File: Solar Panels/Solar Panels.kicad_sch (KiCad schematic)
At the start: 66 parts, among them J2 5040500891

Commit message: Modifications For 2U Panels
Made structural modifications to suit Brett's structure and tried to improve the PCB board based on Parker's suggestions. Schematic is extremely wonky right now but will try to fix it ASAP.
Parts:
- removed CR1, CR10, CR11, CR12, CR13, CR14, CR15, CR16, CR17, CR18, CR19, CR2, CR20, CR21, CR22, CR23, CR24, CR25, CR26, CR27, CR28, CR29, CR3, CR30, CR31, CR32, CR33, CR34, CR35, CR36, CR37, CR38, CR39, CR4, CR40, CR41, CR5, CR6, CR7, CR8, CR9: S3BB, SMB_DIO, symbol Calgary2Space:S3BB-13-F
- removed U1, U10, U11, U12, U13, U14, U15, U16, U17, U18, U19, U2, U20, U21, U22, U23, U24, U3, U4, U5, U6, U7, U8, U9: ~, Calgary2Space:TrisolX Solar Wings, symbol Calgary2Space:Solar_Panels
- added CR1, CR10, CR11, CR12, CR13, CR14, CR15, CR16, CR17, CR18, CR19, CR2, CR20, CR21, CR22, CR23, CR24, CR25, CR26, CR27, CR28, CR29, CR3, CR30, CR31, CR32, CR33, CR34, CR35, CR36, CR37, CR38, CR39, CR4, CR40, CR41, CR42, CR43, CR44, CR45, CR46, CR47, CR48, CR49, CR5, CR50, CR51, CR6, CR7, CR8, CR9: S3B_R1_00001, Solar Panel Library:SMC&slash_DO-214AB_PNJ, symbol Lib:S3B_R1_00001
- added H1, H2, H3, H4, H5, H6, H7, H8: MountingHole_Pad, MountingHole:MountingHole_3.2mm_M3_DIN965_Pad, symbol Mechanical:MountingHole_Pad
- added JP1, JP2, JP3, JP4, JP5, JP6, JP7, JP8: Jumper_2_Open, Jumper:SolderJumper-2_P1.3mm_Open_Pad1.0x1.5mm, symbol Jumper:Jumper_2_Open
- added SC1, SC10, SC11, SC12, SC13, SC14, SC15, SC16, SC17, SC18, SC19, SC2, SC20, SC21, SC22, SC23, SC24, SC25, SC26, SC27, SC28, SC29, SC3, SC30, SC4, SC5, SC6, SC7, SC8, SC9: Solar_Cell, Solar Panel Library:TrisolX Solar Wings, symbol Device:Solar_Cell
- J2: footprint CON_5040500891 -> Solar Panel Library:5040500891
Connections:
- net +VDC: now also CR1.1
- net GND: now also CR11.2, CR12.2, CR20.2, CR26.2, CR31.2, CR36.2, CR41.2, CR46.2, CR51.2, CR6.2, JP1.2 (B), JP2.2 (B), JP3.2 (B), JP4.2 (B), JP5.2 (B), JP6.2 (B), JP7.2 (B), JP8.2 (B), SC12.2 (-), SC15.2 (-), SC18.2 (-), SC21.2 (-), SC24.2 (-), SC27.2 (-), SC3.2 (-), SC30.2 (-), SC6.2 (-), SC9.2 (-)
- new net: CR1.2, CR16.1, CR2.1, CR21.1, CR22.1, CR27.1, CR32.1, CR37.1, CR44.1, CR49.1, CR8.1, SC1.1 (+), SC10.1 (+), SC13.1 (+), SC16.1 (+), SC19.1 (+), SC22.1 (+), SC25.1 (+), SC28.1 (+), SC4.1 (+), SC7.1 (+)
- new net: CR32.2, CR33.1, SC19.2 (-)
- new net: CR13.1, CR14.2, SC8.2 (-)
- new net: CR12.1, CR13.2, SC9.1 (+)
- new net: CR48.1, CR50.2, SC29.2 (-)
- new net: CR48.2, CR51.1, SC30.1 (+)
- new net: CR7.1, CR8.2, SC4.2 (-)
- new net: H4.1, JP4.1 (A)
- new net: CR7.2, CR9.1, SC5.1 (+)
- new net: CR10.1, CR9.2, SC5.2 (-)
- new net: CR37.2, CR38.1, SC22.2 (-)
- new net: H5.1, JP5.1 (A)
- new net: H6.1, JP6.1 (A)
- new net: CR47.2, CR50.1, SC29.1 (+)
- new net: H2.1, JP2.1 (A)
- new net: CR38.2, CR39.1, SC23.1 (+)
- new net: H8.1, JP8.1 (A)
- new net: H1.1, JP1.1 (A)
- new net: CR42.1, CR44.2, SC25.2 (-)
- new net: CR42.2, CR45.1, SC26.1 (+)
- new net: CR5.2, CR6.1, SC3.1 (+)
- new net: CR22.2, CR23.1, SC13.2 (-)
- new net: CR33.2, CR34.1, SC20.1 (+)
- new net: CR34.2, CR35.1, SC20.2 (-)
- new net: CR23.2, CR24.1, SC14.1 (+)
- new net: CR24.2, CR25.1, SC14.2 (-)
- new net: CR17.2, CR18.1, SC11.1 (+)
- new net: CR18.2, CR19.1, SC11.2 (-)
- new net: CR17.1, CR21.2, SC10.2 (-)
- new net: CR28.2, CR29.1, SC17.1 (+)
- new net: CR29.2, CR30.1, SC17.2 (-)
- new net: CR4.2, CR5.1, SC2.2 (-)
- new net: CR25.2, CR26.1, SC15.1 (+)
- new net: CR19.2, CR20.1, SC12.1 (+)
- new net: CR14.1, CR15.2, SC8.1 (+)
- new net: H7.1, JP7.1 (A)
- new net: CR40.2, CR41.1, SC24.1 (+)
- new net: CR43.1, CR45.2, SC26.2 (-)
- new net: CR43.2, CR46.1, SC27.1 (+)
- new net: CR27.2, CR28.1, SC16.2 (-)
- new net: CR30.2, CR31.1, SC18.1 (+)
- new net: CR47.1, CR49.2, SC28.2 (-)
- new net: H3.1, JP3.1 (A)
- new net: CR2.2, CR3.1, SC1.2 (-)
- new net: CR35.2, CR36.1, SC21.1 (+)
- new net: CR39.2, CR40.1, SC23.2 (-)
- new net: CR3.2, CR4.1, SC2.1 (+)
- new net: CR15.1, CR16.2, SC7.2 (-)
- new net: CR10.2, CR11.1, SC6.1 (+)
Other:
- note added: "Mounting Holes"
- moved on the sheet: J2

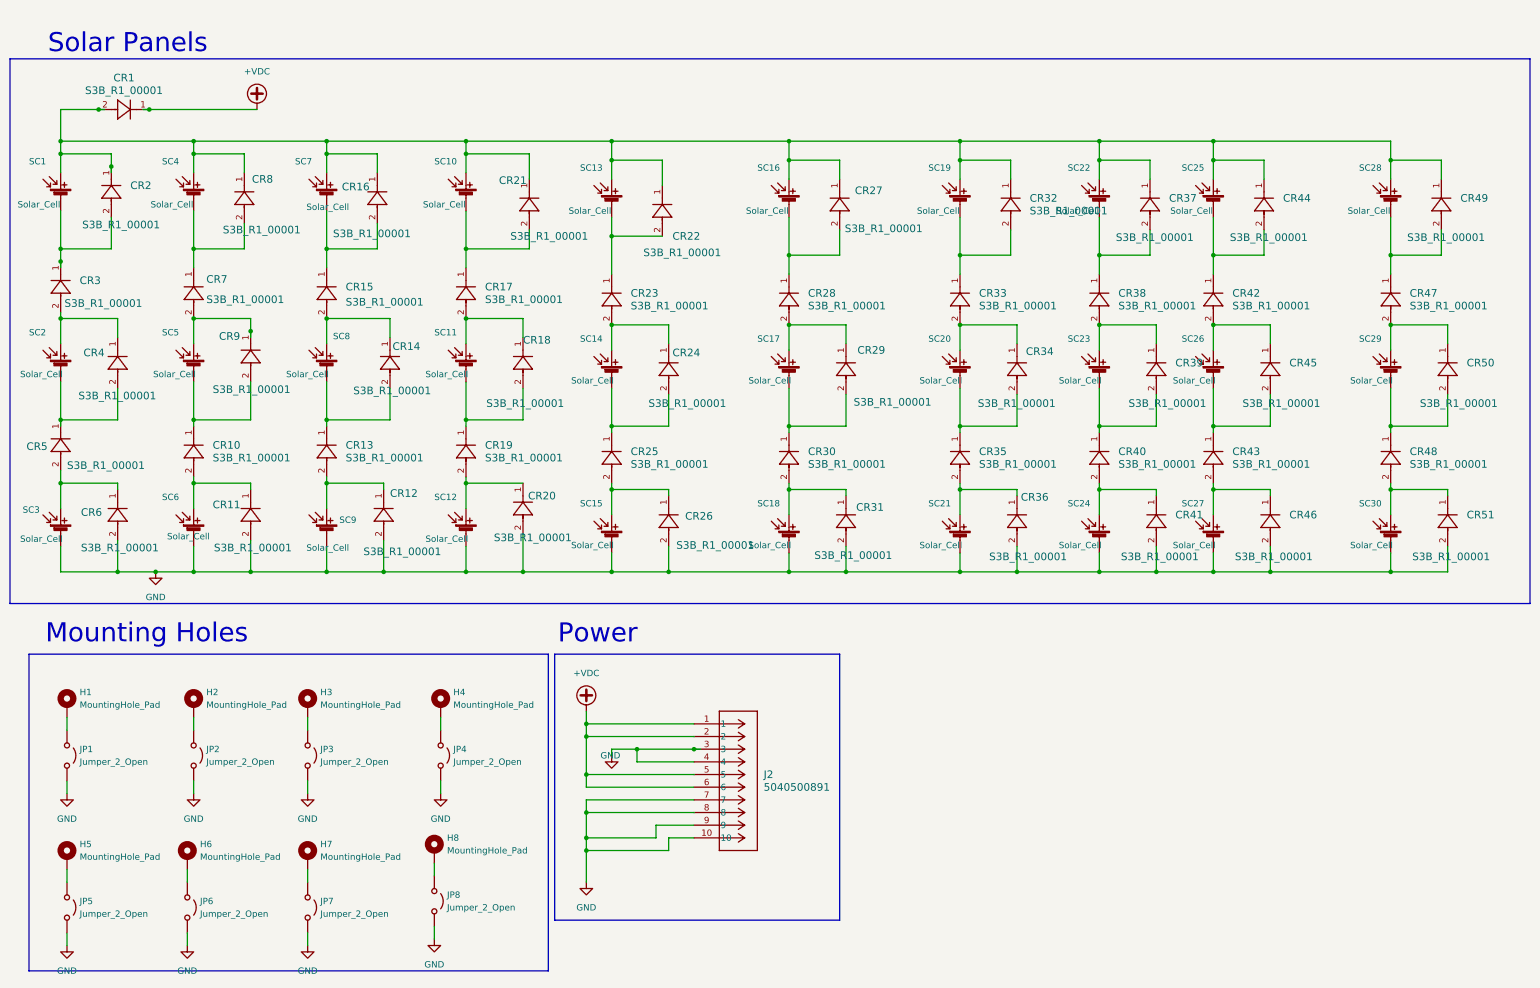
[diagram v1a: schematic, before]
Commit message: Diodes changes and adjusted schematic.
Made the diode changes based off Parker's suggestions and fixed the schematic. Comments are now included within the schematic.
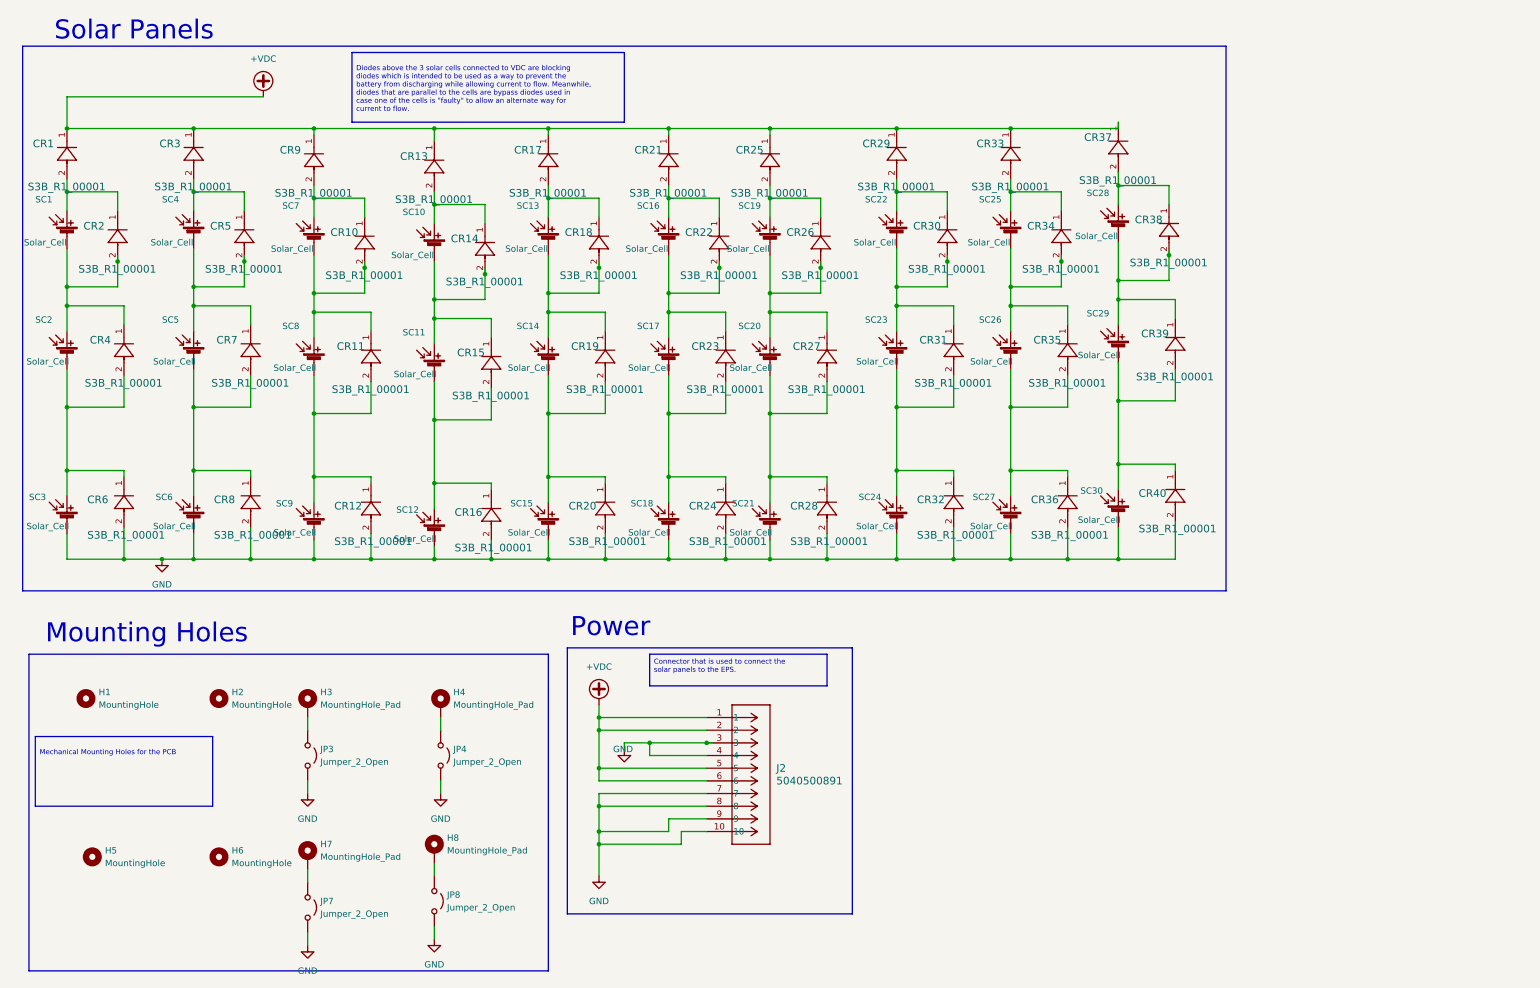
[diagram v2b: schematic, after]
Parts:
- removed CR41, CR42, CR43, CR44, CR45, CR46, CR47, CR48, CR49, CR50, CR51: S3B_R1_00001, Solar Panel Library:SMC&slash_DO-214AB_PNJ, symbol Lib:S3B_R1_00001
- removed H1, H2, H5, H6: MountingHole_Pad, MountingHole:MountingHole_3.2mm_M3_DIN965_Pad, symbol Mechanical:MountingHole_Pad
- removed JP1, JP2, JP5, JP6: Jumper_2_Open, Jumper:SolderJumper-2_P1.3mm_Open_Pad1.0x1.5mm, symbol Jumper:Jumper_2_Open
- added H1, H2, H5, H6: MountingHole, MountingHole:MountingHole_3.2mm_M3_DIN965_Pad, symbol Mechanical:MountingHole
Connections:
- net +VDC: now also CR13.1, CR17.1, CR21.1, CR25.1, CR29.1, CR3.1, CR33.1, CR37.1, CR9.1
- net GND: now also CR16.2, CR24.2, CR28.2, CR32.2, CR40.2, CR8.2; no longer CR11.2, CR26.2, CR31.2
- net at CR12.1, SC9.1 (+): now also CR11.2, SC8.2 (-); no longer CR13.2
- net at SC29.2 (-): now also CR39.2, CR40.1, SC30.1 (+)
- net at CR7.1, SC4.2 (-): now also CR5.2, SC5.1 (+); no longer CR8.2
- net at CR10.1, CR9.2: now also SC7.1 (+); no longer SC5.2 (-)
- net at CR37.2, CR38.1: now also SC28.1 (+); no longer SC22.2 (-)
- net at SC29.1 (+): now also CR38.2, CR39.1, SC28.2 (-)
- net at SC25.2 (-): now also CR34.2, CR35.1, SC26.1 (+)
- net at CR6.1, SC3.1 (+): now also CR4.2, SC2.2 (-); no longer CR5.2
- net at CR22.2, CR23.1: now also SC16.2 (-), SC17.1 (+); no longer SC13.2 (-)
- net at CR33.2, CR34.1: now also SC25.1 (+); no longer SC20.1 (+)
- net at CR23.2, CR24.1: now also SC17.2 (-), SC18.1 (+); no longer SC14.1 (+)
- net at CR17.2, CR18.1: now also SC13.1 (+); no longer SC11.1 (+)
- net at CR18.2, CR19.1: now also SC13.2 (-), SC14.1 (+); no longer SC11.2 (-)
- net at CR29.2, CR30.1: now also SC22.1 (+); no longer SC17.2 (-)
- net at CR25.2, CR26.1: now also SC19.1 (+); no longer SC15.1 (+)
- net at CR19.2, CR20.1: now also SC14.2 (-), SC15.1 (+); no longer SC12.1 (+)
- net at SC24.1 (+): now also CR31.2, CR32.1, SC23.2 (-); no longer CR40.2
- net at SC26.2 (-): now also CR35.2, CR36.1, SC27.1 (+)
- net at CR27.2, CR28.1: now also SC20.2 (-), SC21.1 (+); no longer SC16.2 (-)
- net at CR30.2, CR31.1: now also SC22.2 (-), SC23.1 (+); no longer SC18.1 (+)
- net at CR2.2, SC1.2 (-): now also CR4.1, SC2.1 (+); no longer CR3.1
- net at CR10.2, CR11.1: now also SC7.2 (-), SC8.1 (+); no longer SC6.1 (+)
- new net: CR21.2, CR22.1, SC16.1 (+)
- new net: CR3.2, CR5.1, SC4.1 (+)
- new net: CR15.2, CR16.1, SC11.2 (-), SC12.1 (+)
- new net: CR13.2, CR14.1, SC10.1 (+)
- new net: CR14.2, CR15.1, SC10.2 (-), SC11.1 (+)
- new net: CR26.2, CR27.1, SC19.2 (-), SC20.1 (+)
- new net: CR1.2, CR2.1, SC1.1 (+)
- new net: CR7.2, CR8.1, SC5.2 (-), SC6.1 (+)
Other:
- moved on the sheet: CR4, CR6, J2, SC1, SC2, SC3

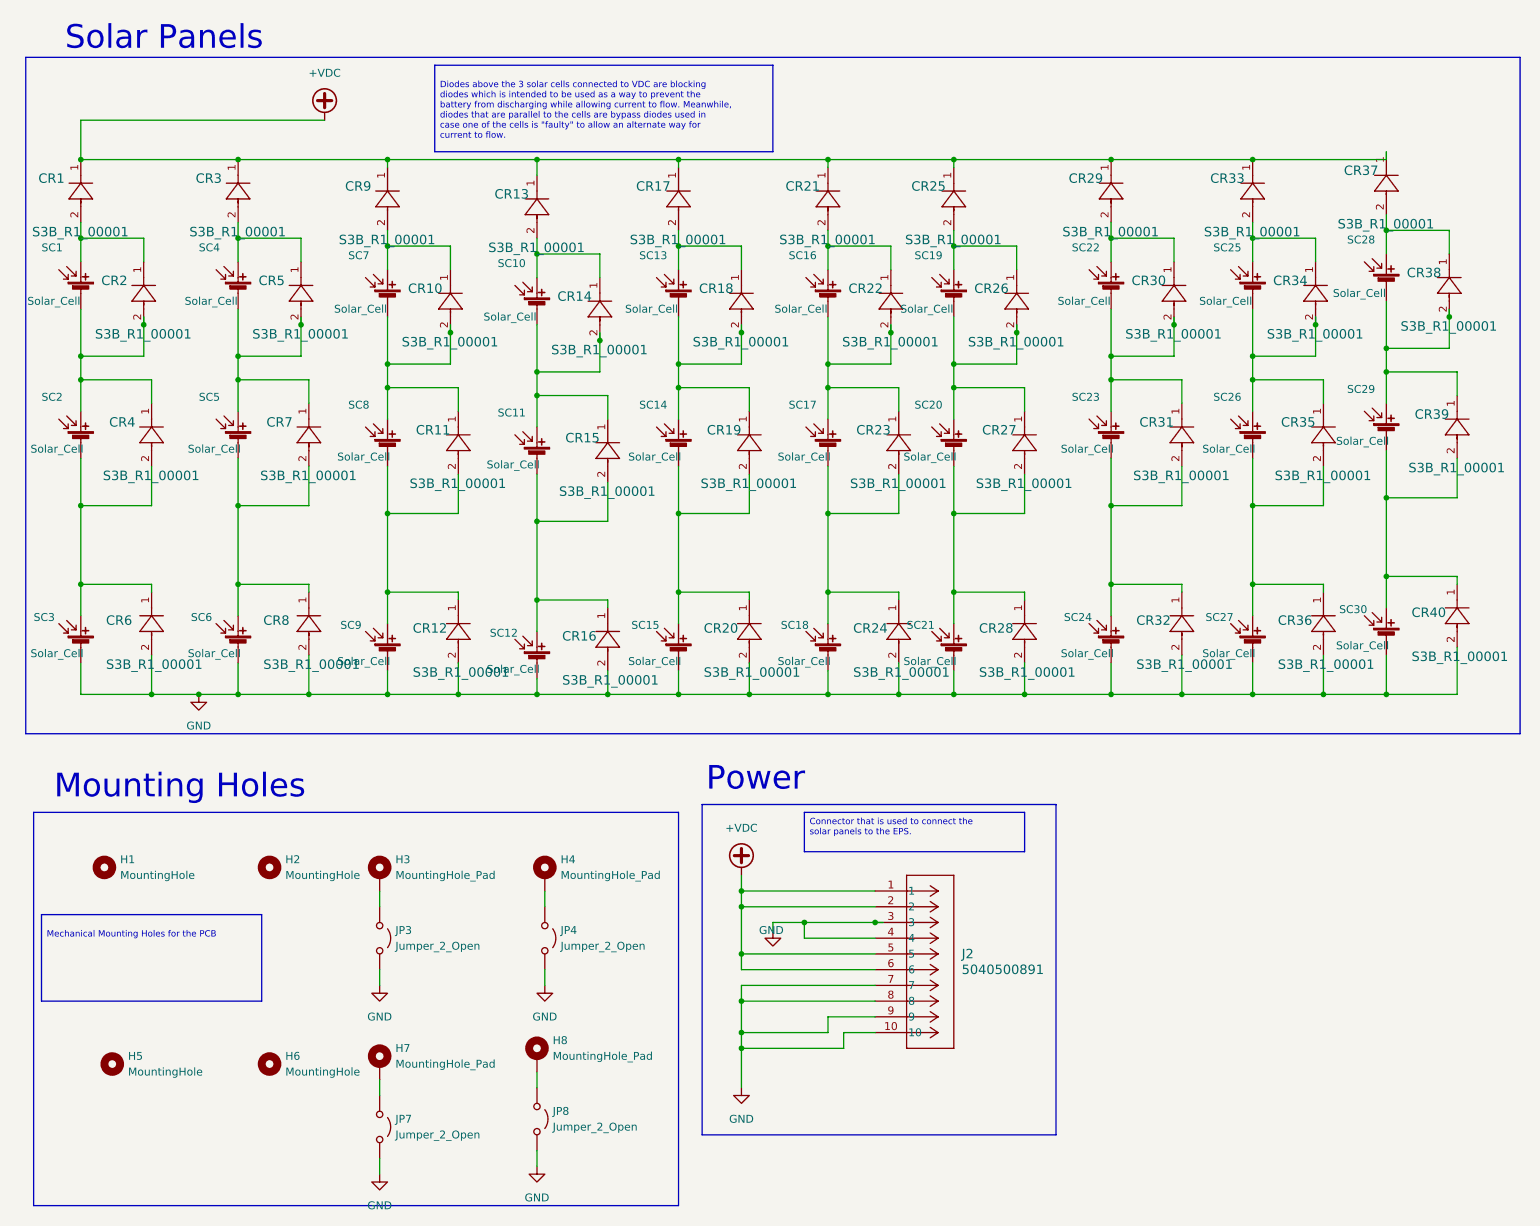
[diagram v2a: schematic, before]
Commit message: Quick Adjustments to Schematic and Routing
Adjusted so there's only one bypass diode for the entire panel. Made changes to the routing as well.
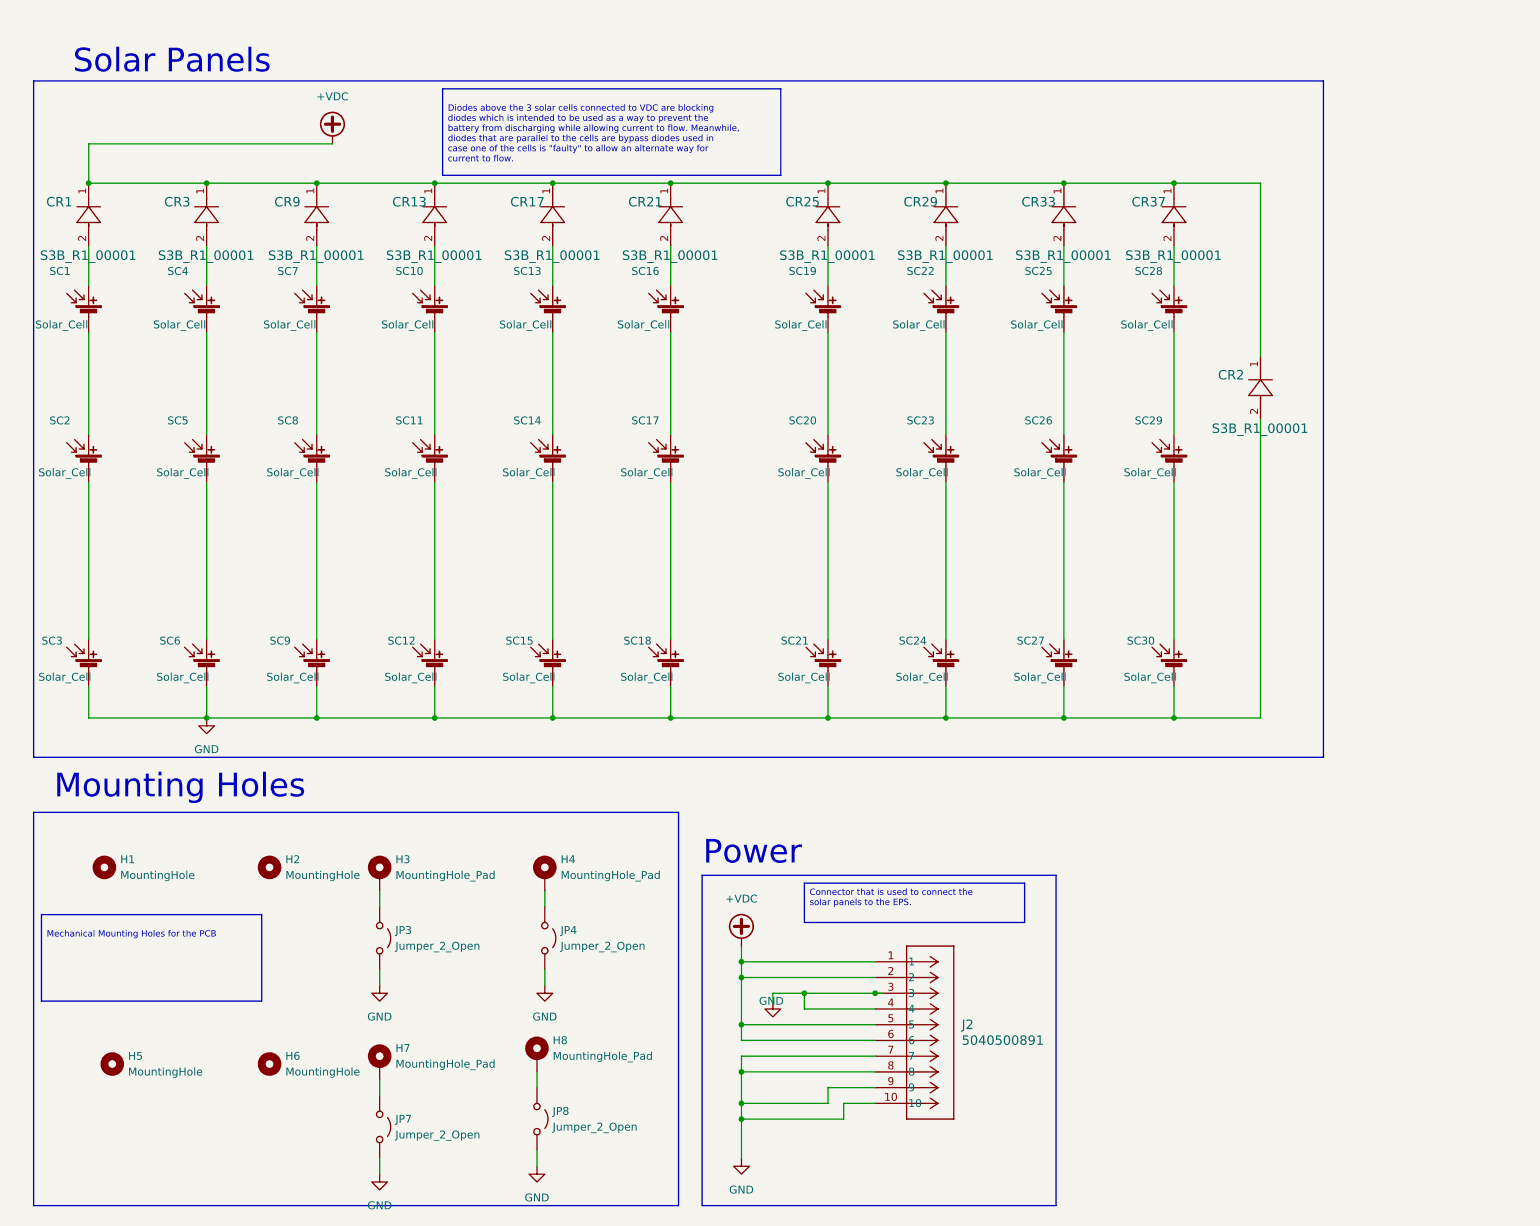
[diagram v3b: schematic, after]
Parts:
- removed CR10, CR11, CR12, CR14, CR15, CR16, CR18, CR19, CR20, CR22, CR23, CR24, CR26, CR27, CR28, CR30, CR31, CR32, CR34, CR35, CR36, CR38, CR39, CR4, CR40, CR5, CR6, CR7, CR8: S3B_R1_00001, Solar Panel Library:SMC&slash_DO-214AB_PNJ, symbol Lib:S3B_R1_00001
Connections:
- net +VDC: now also CR2.1
- net GND: now also CR2.2
- net at CR1.2, SC1.1 (+): no longer CR2.1
- net at SC1.2 (-), SC2.1 (+): no longer CR2.2
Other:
- moved on the sheet: CR1, CR13, CR17, CR21, CR25, CR29, CR3, CR33, CR37, CR9, J2, SC1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
